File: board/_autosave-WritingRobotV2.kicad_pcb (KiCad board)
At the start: 2 copper layers, 61.5 x 55 mm, 7 parts, among them J1 Conn_01x02_Socket, J2 Conn_01x04_Pin, J3 Conn_01x04_Pin, J4 Conn_01x06_Socket

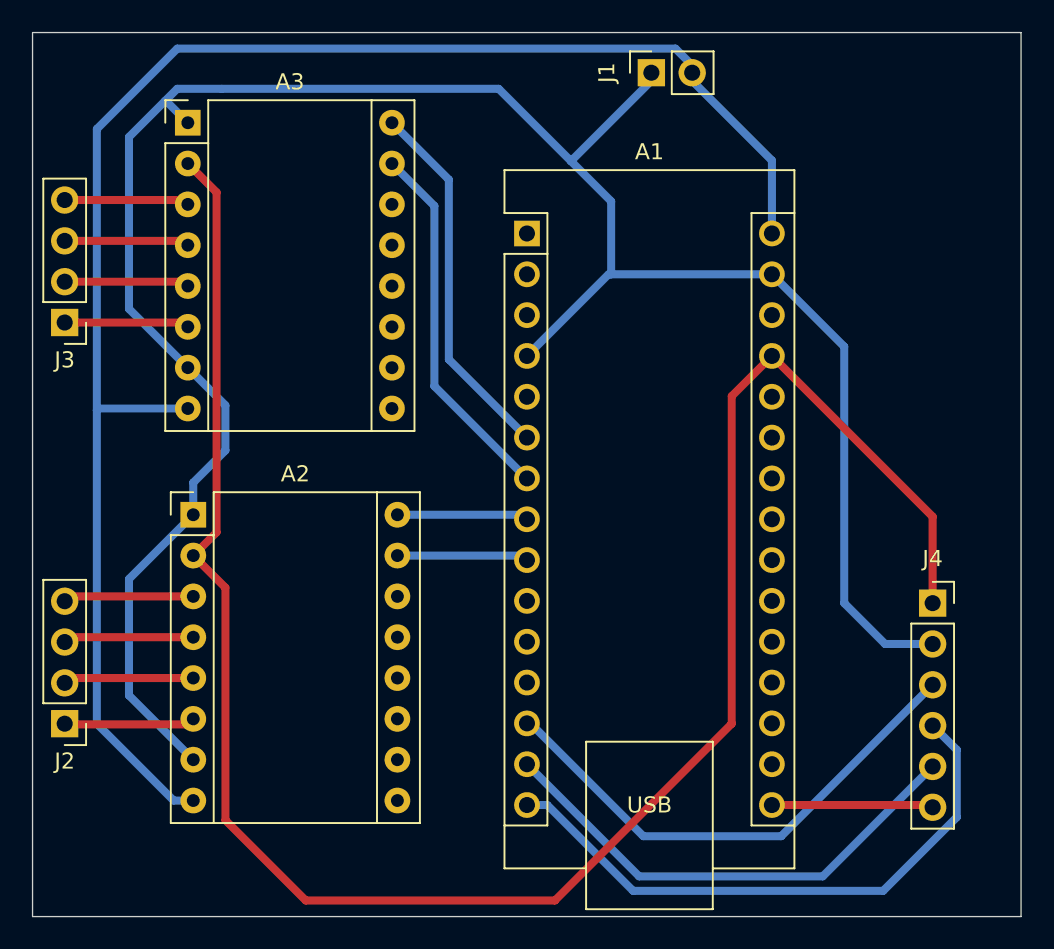
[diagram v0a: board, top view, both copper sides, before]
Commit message: Changed electrical layout Added 3d components to PCB Created photos for DOCU Modified Readme file
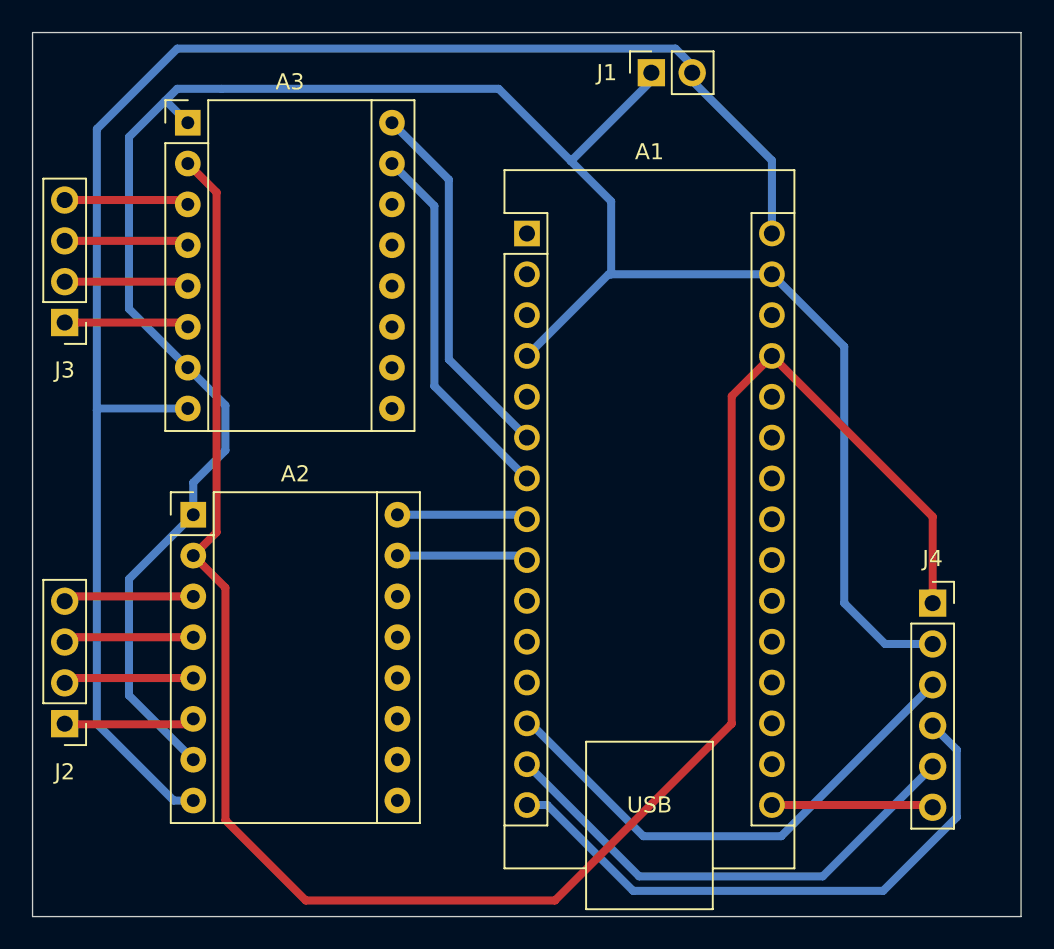
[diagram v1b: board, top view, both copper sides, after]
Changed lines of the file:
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@@
 		(tags "Through hole pin header THT 1x04 2.54mm single row")
 		(property "Reference" "J2"
-			(at 0 -2.33 180)
+			(at 0 -3 180)
 			(layer "F.SilkS")
 			(effects
@@
 		)
 		(property "Value" "Conn_01x04_Pin"
-			(at 0 9.95 180)
-			(layer "F.Fab")
+			(at 8.5 6 180)
+			(layer "F.Fab")
+			(hide yes)
 			(effects
 				(font
@@
 		)
 		(fp_text user "${REFERENCE}"
-			(at 0 3.81 270)
+			(at 0 3.81 -90)
 			(layer "F.Fab")
 			(effects
@@
 		(tags "Through hole socket strip THT 1x06 2.54mm single row")
 		(property "Reference" "J4"
-			(at 0 -2.77 360)
+			(at 0 -2.77 0)
 			(layer "F.SilkS")
 			(effects
@@
 		)
 		(property "Value" "Conn_01x06_Socket"
-			(at 0 15.47 360)
-			(layer "F.Fab")
+			(at 10.5 7 180)
+			(layer "F.Fab")
+			(hide yes)
 			(effects
 				(font
@@
 			)
 		)
+		(model "${KIPRJMOD}/extra_models/a4988-stepper-motor-driver-carrier.step"
+			(hide yes)
+			(offset
+				(xyz -1.25 -19.05 0)
+			)
+			(scale
+				(xyz 1 1 1)
+			)
+			(rotate
+				(xyz 0 0 0)
+			)
+		)
+		(model "${KIPRJMOD}/extra_models/A4988 STEPPER MOTOR DRIVER CARRIER--3DModel-STEP-56544.STEP"
+			(offset
+				(xyz 6.2 -8.9 0)
+			)
+			(scale
+				(xyz 1 1 1)
+			)
+			(rotate
+				(xyz -90 0 0)
+			)
+		)
 	)
 	(footprint "Connector_PinSocket_2.54mm:PinSocket_1x02_P2.54mm_Vertical"
@@
 		(tags "Through hole socket strip THT 1x02 2.54mm single row")
 		(property "Reference" "J1"
-			(at 0 -2.77 270)
+			(at 0 -2.77 0)
 			(layer "F.SilkS")
 			(effects
@@
 		)
 		(property "Value" "Conn_01x02_Socket"
-			(at 0 5.31 270)
-			(layer "F.Fab")
+			(at 3.5 2 0)
+			(layer "F.Fab")
+			(hide yes)
 			(effects
 				(font
@@
 		)
 		(fp_text user "${REFERENCE}"
-			(at 0 1.27 360)
+			(at 0 1.27 0)
 			(layer "F.Fab")
 			(effects
@@
 		(tags "Through hole pin header THT 1x04 2.54mm single row")
 		(property "Reference" "J3"
-			(at 0 -2.33 180)
+			(at 0 -2.96 180)
 			(layer "F.SilkS")
 			(effects
@@
 			)
 			(layer "F.Fab")
-		)
-		(fp_text user "${REFERENCE}"
-			(at 0 3.81 270)
-			(layer "F.Fab")
-			(effects
-				(font
-					(size 1 1)
-					(thickness 0.15)
-				)
-			)
 		)
 		(pad "1" thru_hole rect
@@
 		)
 		(property "Value" "Arduino_Nano_Every"
-			(at 24.24 18 90)
+			(at 8.24 18.5 -90)
 			(layer "F.Fab")
 			(effects
@@
 			(rotate
 				(xyz 0 0 0)
+			)
+		)
+		(model "${KIPRJMOD}/extra_models/Arduino Nano.STEP"
+			(offset
+				(xyz 7.7 -17.9 0)
+			)
+			(scale
+				(xyz 1 1 1)
+			)
+			(rotate
+				(xyz -90 0 180)
 			)
 		)
@@
 			)
 		)
+		(model "${KIPRJMOD}/extra_models/a4988-stepper-motor-driver-carrier.step"
+			(hide yes)
+			(offset
+				(xyz -1.25 -19.05 0)
+			)
+			(scale
+				(xyz 1 1 1)
+			)
+			(rotate
+				(xyz 0 0 0)
+			)
+		)
+		(model "${KIPRJMOD}/extra_models/A4988 STEPPER MOTOR DRIVER CARRIER--3DModel-STEP-56544.STEP"
+			(offset
+				(xyz 6.2 -8.9 0)
+			)
+			(scale
+				(xyz 1 1 1)
+			)
+			(rotate
+				(xyz -90 0 0)
+			)
+		)
